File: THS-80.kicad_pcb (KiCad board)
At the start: 4 copper layers, 101.6 x 101.6 mm, 118 parts, among them J1 USB_B_Micro, J10 CTC Header, J2 RC80 Bus, J3 RC80 Expansion, J4 IDE, J5 JTAG, J6 PMOD, J7 PIO Header, J8 Port B, J9 Port A, SW1 Reset, SW2 SW_DIP_x06, SW3 User PB, U1 MAX40203AUK, U10 AP7381-33SA, U11 TXS0108EPW, U12 74HCT3G04, U2 DS1813R-5+T&R, U3 EPM7064STC100, U4 Z84C0010AEG, U5 IS62C5128BL-45TLI, U6 SST39SF040, U7 Z84C2010AEG, U8 Z84C4310AEG, U9 Z84C3010AEG, X1 CFPS-72 50mhz

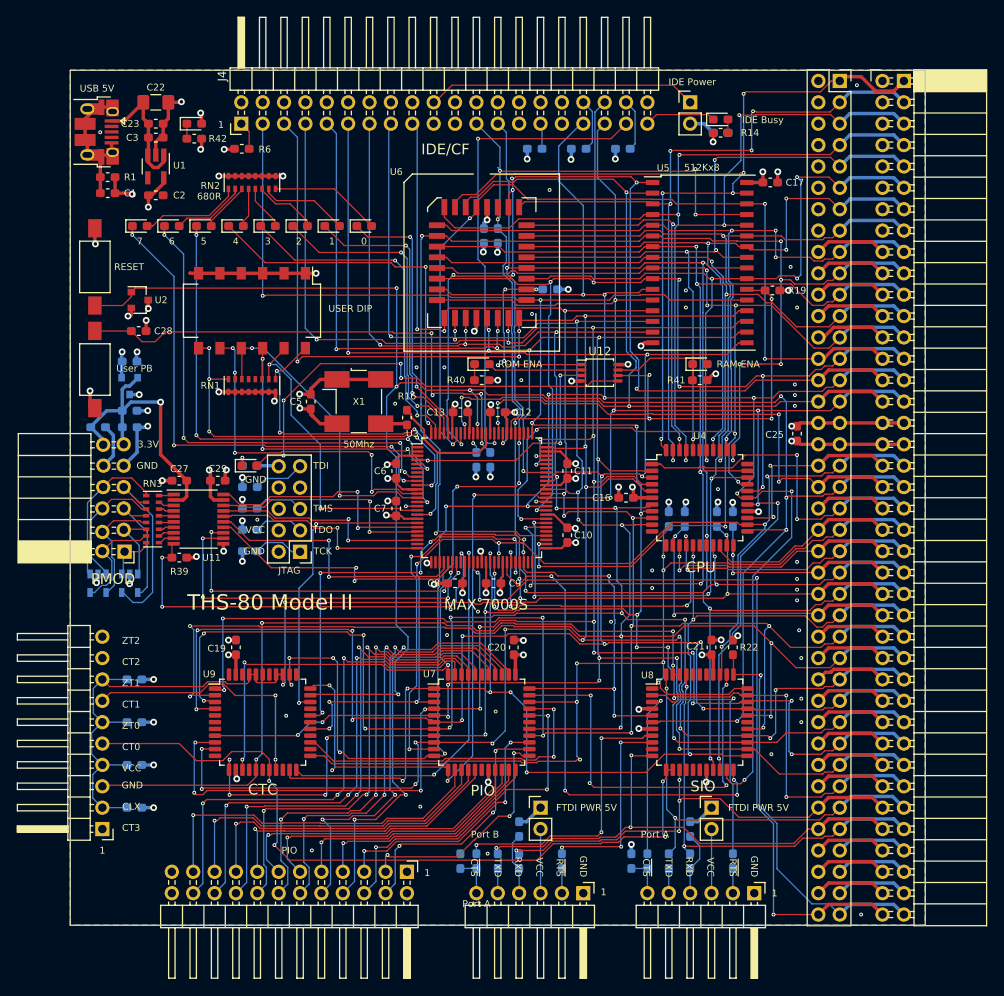
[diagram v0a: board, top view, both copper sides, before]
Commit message: fixes for CTC and additional clocks
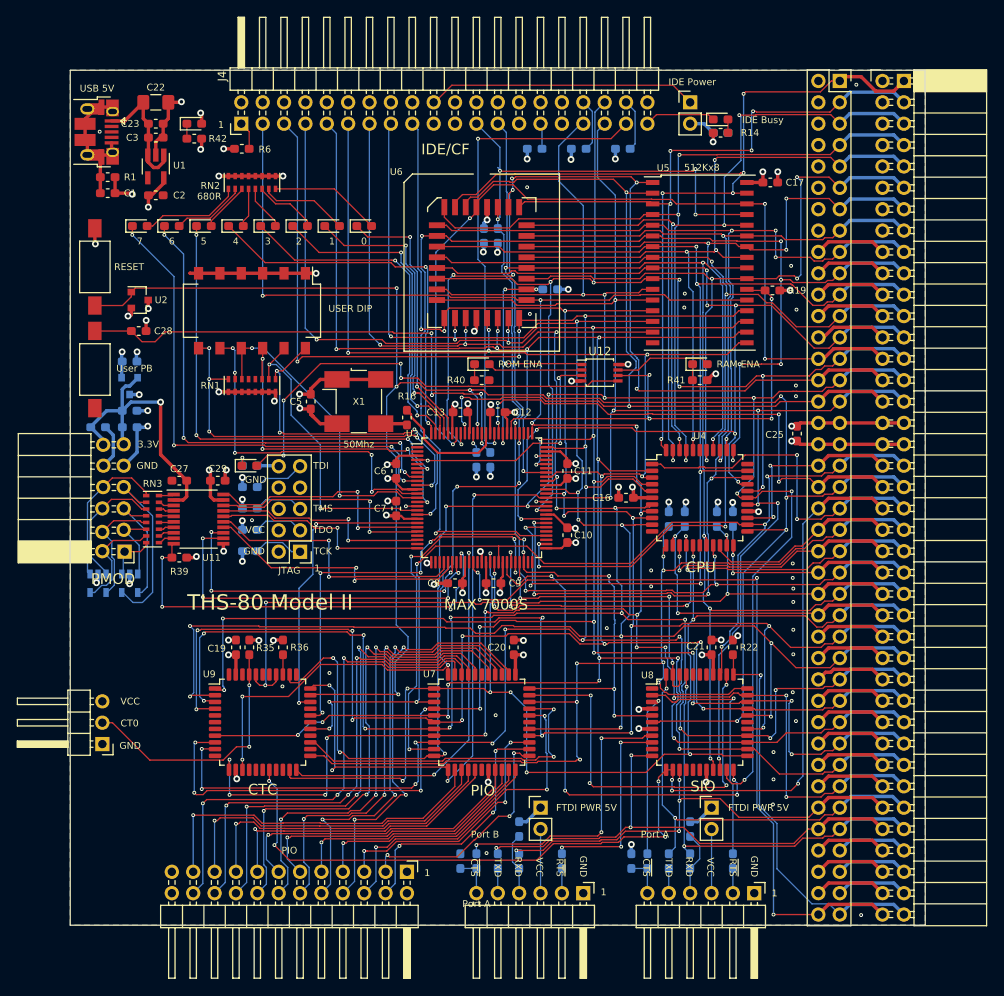
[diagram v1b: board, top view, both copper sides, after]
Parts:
- removed R37, R38: 10K, Resistor_SMD:R_0603_1608Metric_Pad1.05x0.95mm_HandSolder
- J10: value CTC Header -> CT0; footprint Connector_PinHeader_2.54mm:PinHeader_1x10_P2.54mm_Horizontal -> Connector_PinHeader_2.54mm:PinHeader_1x03_P2.54mm_Horizontal
- R35, R36: moved to F.Cu
- moved R35 23.4 mm to (122.9, 100.3), turned to 270 degrees
- moved R36 22.5 mm to (126.9, 100.3), turned to 270 degrees
- moved J10 10.1 mm to (105.4, 111.8)
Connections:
- J10 pad 1: VCC -> GND
- J10 pad 2: /CLK_U -> /CT0
- J10 pad 3: /Peripherals/CLK_A -> VCC
- J2 pad 42: /~CLK2 -> /CLK2
- J3 pad 42: /~CLK2 -> /CLK2
- R35 pad 2: /CLK_U -> /CT0
- R36 pad 2: /CLK_U -> /CT3
- U8 pad 12: /Peripherals/CLK_B -> /CLK2
- U8 pad 13: /Peripherals/CLK_B -> /CLK2
- U8 pad 42: /Peripherals/CLK_A -> /CLK_U
- U8 pad 43: /Peripherals/CLK_A -> /CLK_U
- U9 pad 16: /Peripherals/CLK_A -> (no net)
- U9 pad 18: /Peripherals/CLK_B -> /CLK2
- U9 pad 19: /Peripherals/CLK_C -> (no net)
- U9 pad 36: /CLK_U -> /CT3
- U9 pad 41: /CLK_U -> /CT0
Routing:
- net /CLK2: track 0.00 -> 127.5 mm, vias 0 -> 7
- net /Peripherals/CLK_A: track 93.3 -> 0.00 mm, vias 4 -> 0
- net /Peripherals/CLK_B: track 89.7 -> 0.00 mm, vias 4 -> 0
- net /CT0: track 0.00 -> 30.9 mm, vias 0 -> 2
- net /Peripherals/CLK_C: track 30.8 -> 0.00 mm, vias 2 -> 0
- net /CLK_U: track 98.5 -> 80.0 mm, vias 4 -> 6
- net /~CLK2: track 8.62 -> 0.00 mm
- net GND: track 134.2 -> 128.6 mm, vias 87 -> 75
- net VCC: track 143.6 -> 140.9 mm, vias 48 -> 46
- net /~RD: track 237.7 -> 235.2 mm
- net /CT3: track 0.00 -> 2.36 mm
- net /A1: track 257.0 -> 254.8 mm, vias 15 -> 13
- net /~M1: track 127.6 -> 126.6 mm, vias 9 -> 7
- net /~NMI: track 38.3 -> 37.6 mm
- net /Peripherals/IEO_1: track 38.8 -> 39.3 mm
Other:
- board text removed: "CLX"
- board text removed: "CT1"
- board text removed: "CT2"
- board text removed: "CT3"
- board text removed: "ZT0"
- board text removed: "ZT1"
- board text removed: "ZT2"

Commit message: swapped CTC and PIO
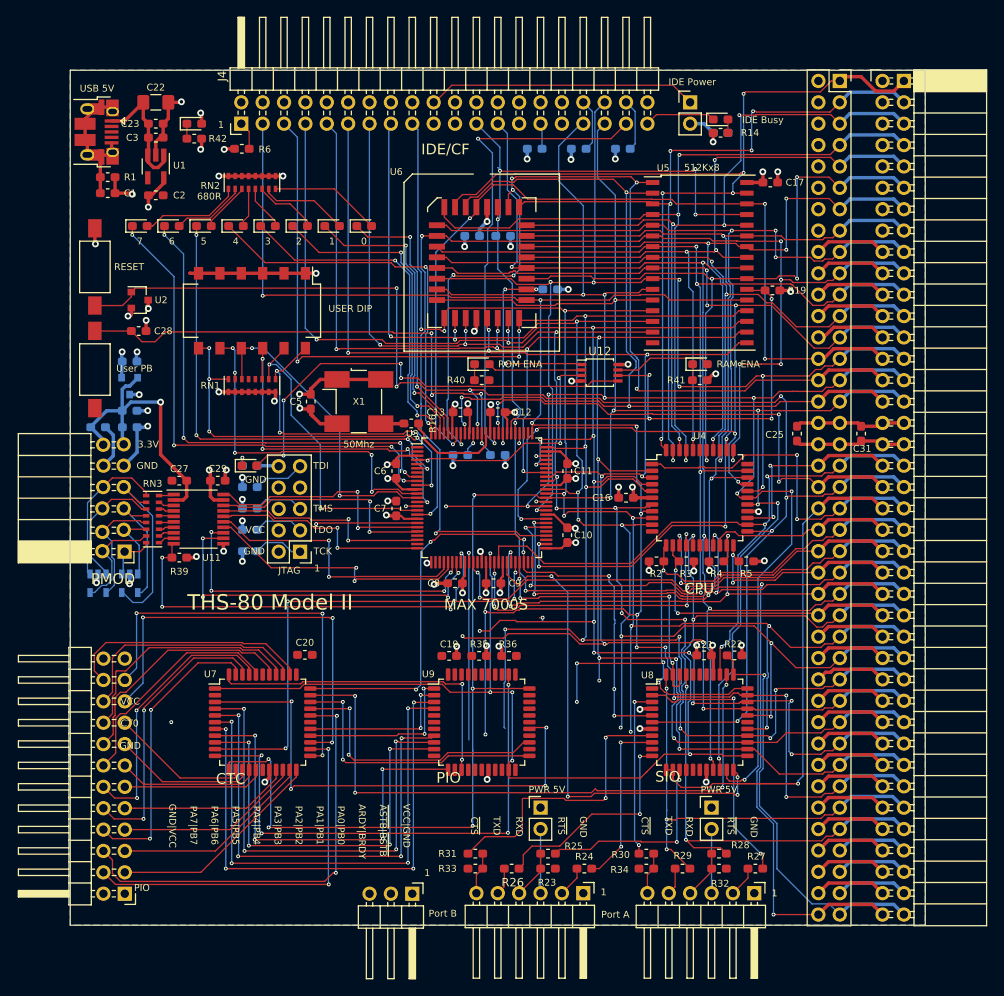
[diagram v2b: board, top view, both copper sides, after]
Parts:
- added C31: 100nF, Capacitor_SMD:C_0603_1608Metric_Pad1.05x0.95mm_HandSolder, F.Cu at (195.6, 74.9)
- J8: value Port B -> Port A
- R2, R24, R25, R26, R27, R28, R29, R3, R30, R32, R33, R34, R4, R5: moved to F.Cu
- R23: value 2K2 -> 100K; moved to F.Cu
- R31: value 100K -> 2K2; moved to F.Cu
- moved J10 40.9 mm to (142.2, 129.6), turned to 270 degrees
- moved J7 33.6 mm to (108.1, 129.6), turned to 180 degrees
- moved R35 27.3 mm to (150.2, 101.3), turned to 180 degrees
- moved R36 26.9 mm to (153.7, 101.3), turned to 0 degrees
- moved U7 26.0 mm to (124.5, 109.2)
- moved U9 26.0 mm to (150.5, 109.2)
- moved C19 25.4 mm to (146.6, 101.3), turned to 180 degrees
- moved C20 24.8 mm to (129.5, 101.2), turned to 0 degrees
- moved R24 7.80 mm to (162.7, 126.6), turned to 0 degrees
- moved R25 6.03 mm to (158.4, 124.8), turned to 0 degrees
- moved R31 5.97 mm to (149.7, 124.8), turned to 180 degrees
- moved R32 5.82 mm to (178.7, 126.6), turned to 180 degrees
- moved R5 5.26 mm to (181.9, 90.1), turned to 180 degrees
- moved R2 5.22 mm to (171.3, 90.1), turned to 0 degrees
- moved R3 5.02 mm to (174.8, 90.1), turned to 180 degrees
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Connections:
- net Net-(J9-Pad2) renamed /Peripherals/RTA
- net Net-(J9-Pad4) renamed /Peripherals/RA
- net Net-(J9-Pad5) renamed /Peripherals/TA
- net Net-(J9-Pad6) renamed /Peripherals/CTA
- J7 pad 10: /Peripherals/PB1 -> /Peripherals/PB6
- J7 pad 11: /Peripherals/PA2 -> /Peripherals/PA4
- J7 pad 12: /Peripherals/PB2 -> /Peripherals/PB5
- J7 pad 13: /Peripherals/PA3 -> /Peripherals/PA5
- J7 pad 14: /Peripherals/PB3 -> /Peripherals/PB4
- J7 pad 15: /Peripherals/PA4 -> /Peripherals/PA6
- J7 pad 16: /Peripherals/PB4 -> /Peripherals/PB3
- J7 pad 17: /Peripherals/PA5 -> /Peripherals/PA7
- J7 pad 18: /Peripherals/PB5 -> /Peripherals/PB2
- J7 pad 19: /Peripherals/PA6 -> /Peripherals/ARDY
- J7 pad 20: /Peripherals/PB6 -> /Peripherals/PB1
- J7 pad 21: /Peripherals/PA7 -> /Peripherals/~ASTB
- J7 pad 22: /Peripherals/PB7 -> /Peripherals/PB0
- J7 pad 3: /Peripherals/~ASTB -> /Peripherals/PA0
- J7 pad 5: /Peripherals/ARDY -> /Peripherals/PA1
- J7 pad 7: /Peripherals/PA0 -> /Peripherals/PA2
- J7 pad 8: /Peripherals/PB0 -> /Peripherals/PB7
- J7 pad 9: /Peripherals/PA1 -> /Peripherals/PA3
- J8 pad 2: Net-(J8-Pad2) -> /Peripherals/RTB
- J8 pad 4: Net-(J8-Pad4) -> /Peripherals/RB
- J8 pad 5: Net-(J8-Pad5) -> /Peripherals/TB
- J8 pad 6: Net-(J8-Pad6) -> /Peripherals/CTB
- R23 pad 1: Net-(J8-Pad2) -> VCC
- R23 pad 2: /Peripherals/~RTSB -> /Peripherals/RB
- R24 pad 1: Net-(J8-Pad4) -> /Peripherals/RTB
- R24 pad 2: /TXB -> /Peripherals/~RTSB
- R25 pad 1: Net-(J8-Pad5) -> /Peripherals/RB
- R25 pad 2: /RXB -> /Peripherals/RXB
- R26 pad 1: Net-(J8-Pad6) -> /Peripherals/TB
- R26 pad 2: /Peripherals/~CTSB -> /Peripherals/TXB
- R31 pad 1: VCC -> /Peripherals/CTB
- R31 pad 2: Net-(J8-Pad4) -> /Peripherals/~CTSB
- R33 pad 1: Net-(J8-Pad6) -> /Peripherals/CTB
- U8 pad 11: /RXB -> /Peripherals/TXB
- U8 pad 14: /TXB -> /Peripherals/RXB
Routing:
- net /CLK2: track 127.5 -> 69.8 mm, vias 7 -> 2
- net /D1: track 246.7 -> 190.2 mm
- net /~RD: track 235.2 -> 181.6 mm, vias 11 -> 8
- net /D0: track 242.4 -> 189.3 mm, vias 14 -> 13
- net /RXB: track 61.3 -> 8.62 mm, vias 3 -> 0
- net /~RESET: track 222.6 -> 171.4 mm, vias 9 -> 8
- net /TXB: track 54.8 -> 8.62 mm, vias 4 -> 0
- net /CLK_U: track 80.0 -> 35.0 mm, vias 6 -> 4
- net /CT0: track 30.9 -> 0.00 mm, vias 2 -> 0
- net /Peripherals/PB4: track 56.5 -> 27.4 mm, vias 3 -> 0
- net /Peripherals/PB3: track 55.4 -> 28.5 mm, vias 3 -> 0
- net /Peripherals/IEO_0: track 47.9 -> 74.6 mm
- net /Peripherals/TXB: track 0.00 -> 26.4 mm, vias 0 -> 2
- net /Peripherals/PB5: track 57.7 -> 32.3 mm, vias 3 -> 2
- net /Peripherals/PA7: track 42.1 -> 16.8 mm, vias 1 -> 0
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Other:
- board text added: "ARDY|BRDY"
- board text added: "GND|VCC"
- board text added: "PA0|PB0"
- board text added: "PA1|PB1"
- board text added: "PA2|PB2"
- board text added: "PA3|PB3"
- board text added: "PA4|PB4"
- board text added: "PA5|PB5"
- board text added: "PA6|PB6"
- board text added: "PA7|PB7"
- board text added: "PWR 5V"
- board text added: "VCC|GND"
- board text added: "~ASTB~|~BSTB~"
- board text removed: "FTDI PWR 5V"

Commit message: lots of fixes
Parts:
- removed R13: 10K, Resistor_SMD:R_0603_1608Metric_Pad1.05x0.95mm_HandSolder
- C18, R15, R20, R21, R7, R8, R9: moved to F.Cu
- J5: footprint Connector_PinHeader_2.54mm:PinHeader_2x05_P2.54mm_Vertical -> Connector_Multicomp:Multicomp_MC9A12-1034_2x05_P2.54mm_Vertical
- moved R15 21.8 mm to (134.9, 97.0)
- moved D2 20.4 mm to (134.9, 95.2)
- moved R12 10.3 mm to (132.3, 82.0), turned to 180 degrees
- moved R11 9.96 mm to (132.3, 87.1), turned to 180 degrees
- moved R10 9.96 mm to (132.3, 92.2), turned to 180 degrees
- moved C18 8.57 mm to (150.4, 42.9)
- moved R21 8.56 mm to (153.9, 42.9)
- moved J5 3.30 mm to (128.9, 92.3), turned to 90 degrees
- moved R20 3.18 mm to (161.8, 57.8)
- moved JP2 1.78 mm to (159.3, 119.4)
- moved R26 1.78 mm to (155.8, 126.6)
- moved R28 1.78 mm to (180.5, 124.8)
- moved R29 1.78 mm to (176.1, 126.6)
- moved R32 1.78 mm to (180.5, 126.6)
- moved J8 1.78 mm to (164.3, 129.5)
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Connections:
- R12 pad 2: /CPLD/TDO -> /CPLD/TDI
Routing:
- net /D7: track 269.0 -> 0.00 mm, vias 17 -> 0
- net /D6: track 266.5 -> 0.00 mm, vias 14 -> 0
- net /D5: track 260.0 -> 0.00 mm, vias 19 -> 0
- net /A0: track 259.2 -> 0.00 mm, vias 12 -> 0
- net /A1: track 255.4 -> 0.00 mm, vias 14 -> 0
- net /D4: track 251.8 -> 0.00 mm, vias 15 -> 0
- net /D3: track 251.3 -> 0.00 mm, vias 14 -> 0
- net /D2: track 228.3 -> 0.00 mm, vias 16 -> 0
- net /D1: track 190.2 -> 0.00 mm, vias 13 -> 0
- net /D0: track 189.3 -> 0.00 mm, vias 13 -> 0
- net /~RD: track 181.6 -> 0.00 mm, vias 8 -> 0
- net /~RESET: track 171.4 -> 0.00 mm, vias 8 -> 0
- net /~WR: track 152.9 -> 0.00 mm, vias 8 -> 0
- net /~IORQ: track 149.7 -> 0.00 mm, vias 7 -> 0
- net /A6: track 143.0 -> 0.00 mm, vias 7 -> 0
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
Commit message: rerouting
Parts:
- moved R17 1.34 mm to (148.1, 78.8)
- moved R18 1.33 mm to (152.4, 78.8)
- moved C11 1.27 mm to (160.7, 80.5)
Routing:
- net /D5: track 0.00 -> 133.3 mm, vias 0 -> 6
- net /D6: track 0.00 -> 128.3 mm, vias 0 -> 4
- net /D4: track 0.00 -> 125.7 mm, vias 0 -> 3
- net /D3: track 0.00 -> 122.3 mm, vias 0 -> 3
- net /D1: track 0.00 -> 112.3 mm, vias 0 -> 4
- net /D2: track 0.00 -> 111.9 mm, vias 0 -> 5
- net /A16: track 0.00 -> 109.9 mm, vias 0 -> 5
- net /~WR: track 0.00 -> 101.6 mm, vias 0 -> 6
- net /D0: track 0.00 -> 101.4 mm, vias 0 -> 4
- net /~RD: track 0.00 -> 92.7 mm, vias 0 -> 6
- net /D7: track 0.00 -> 92.2 mm, vias 0 -> 4
- net /A15: track 0.00 -> 70.9 mm, vias 0 -> 2
- net /A1: track 0.00 -> 69.1 mm, vias 0 -> 2
- net /A0: track 0.00 -> 68.5 mm, vias 0 -> 2
- net /A2: track 0.00 -> 66.5 mm, vias 0 -> 2
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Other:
- board size 101.6 x 101.6 mm -> 101.6 x 102.1 mm

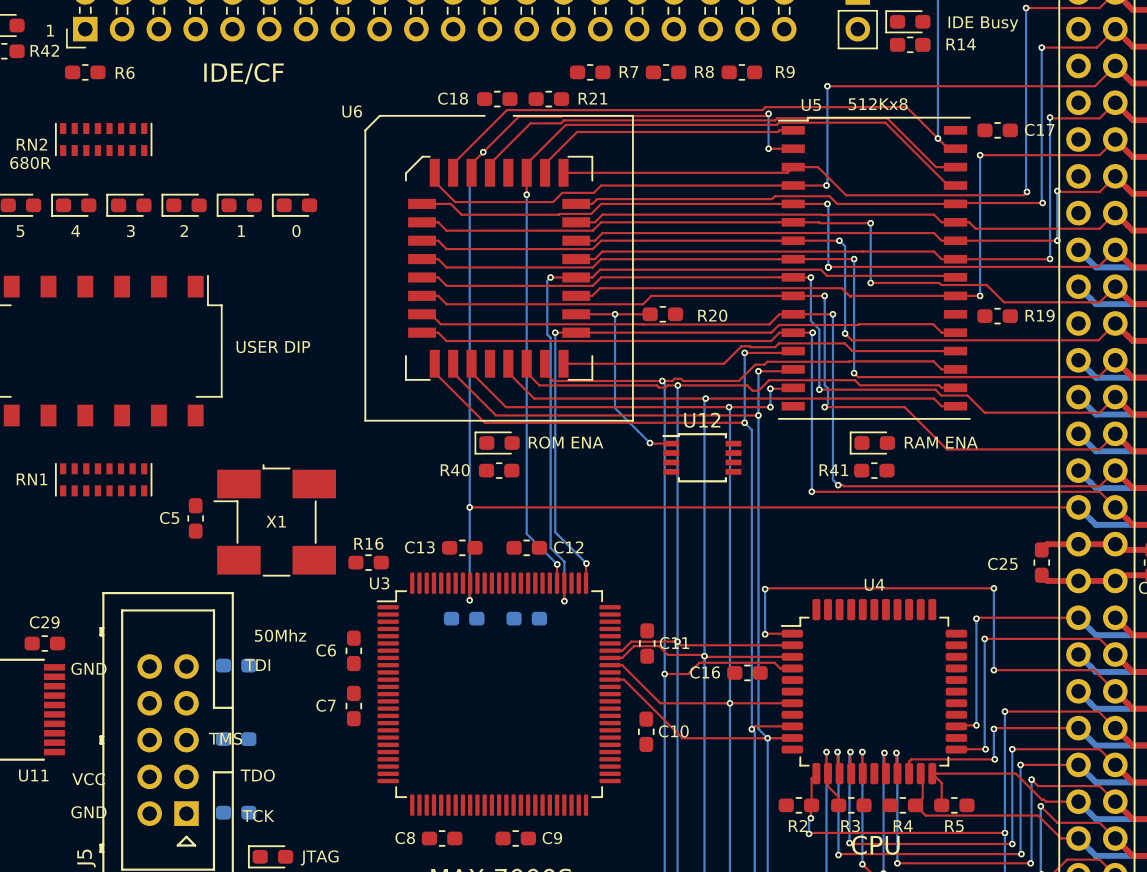
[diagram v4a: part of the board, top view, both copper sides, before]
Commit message: replaced VCC with 5V, fixed ROM footprint
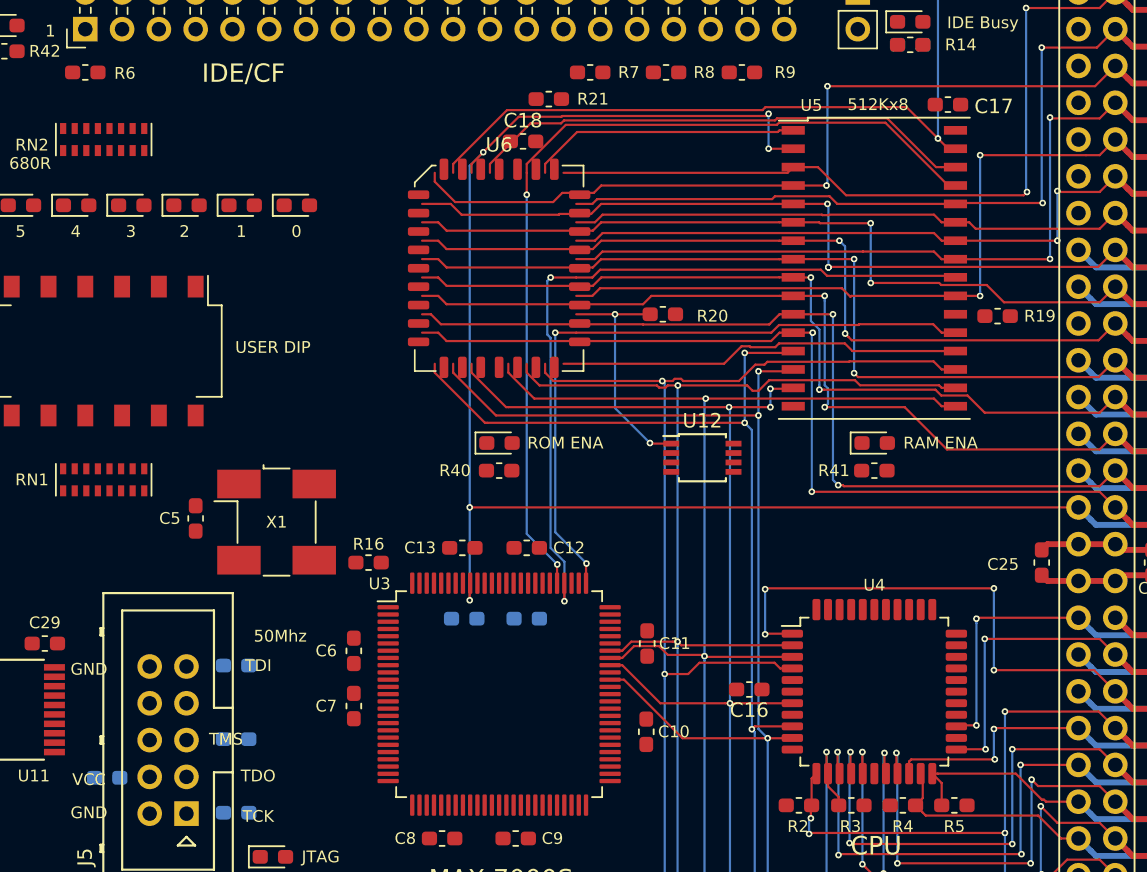
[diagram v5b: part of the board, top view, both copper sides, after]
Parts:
- added C30: 100nF, Capacitor_SMD:C_0603_1608Metric_Pad1.05x0.95mm_HandSolder, B.Cu at (123.4, 89.8)
- U6: footprint Package_LCC:PLCC-32_SMD-Socket -> Package_LCC:PLCC-32_11.4x14.0mm_P1.27mm
- moved C17 3.86 mm to (181.5, 43.3), turned to 180 degrees
- moved C18 3.42 mm to (152.1, 45.8), turned to 0 degrees
- moved C16 1.15 mm to (167.8, 83.7)
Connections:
- net VCC renamed +5V
- J1 pad 4: (no net) -> GND
- J1 pad 5: Net-(C1-Pad1) -> GND
- R25 pad 2: /Peripherals/RXB -> /RXB
- R26 pad 2: /Peripherals/TXB -> /TXB
- U8 pad 11: /Peripherals/TXB -> /TXB
- U8 pad 14: /Peripherals/RXB -> /RXB
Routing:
- added copper zone on In2.Cu, net VCC
- removed copper zone on In2.Cu, net +5V

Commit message: routing checkpoint
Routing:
- net /D7: track 92.2 -> 113.0 mm, vias 4 -> 6
- net /D0: track 101.4 -> 115.1 mm, vias 4 -> 6
- net /D4: track 125.7 -> 138.7 mm, vias 3 -> 6
- net /D3: track 122.3 -> 134.3 mm, vias 3 -> 5
- net /D1: track 112.3 -> 122.7 mm, vias 4 -> 6
- net /D2: track 111.9 -> 103.3 mm
- net /D5: track 133.3 -> 132.7 mm
